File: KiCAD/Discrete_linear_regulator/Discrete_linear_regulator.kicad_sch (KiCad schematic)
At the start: 40 parts, among them J1 Conn_01x06, Q1 PZT2222AT3G, Q10 BC857, Q11 BC857, Q2 BC857, Q3 BC857, Q4 PZT2222AT3G, Q5 PZT2907AT3G, Q8 PZT2907AT3G, U1 LM4562

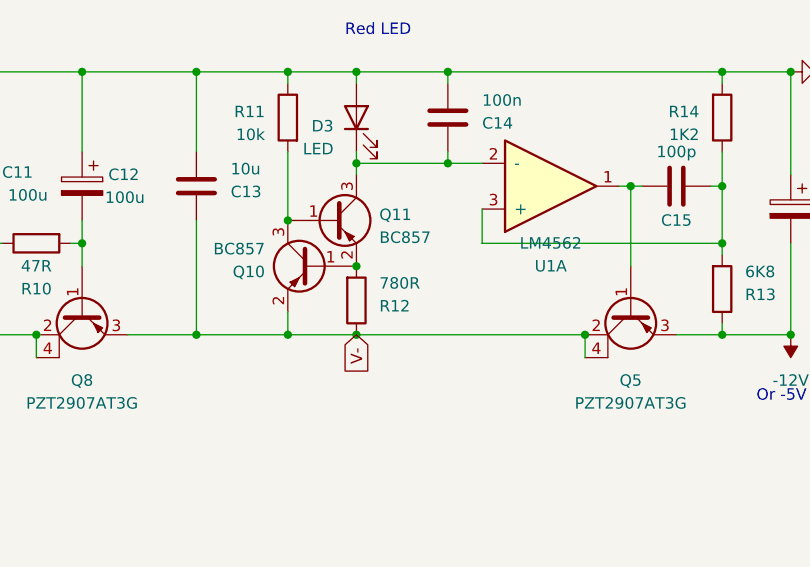
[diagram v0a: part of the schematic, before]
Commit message: Linear regulator schematic update
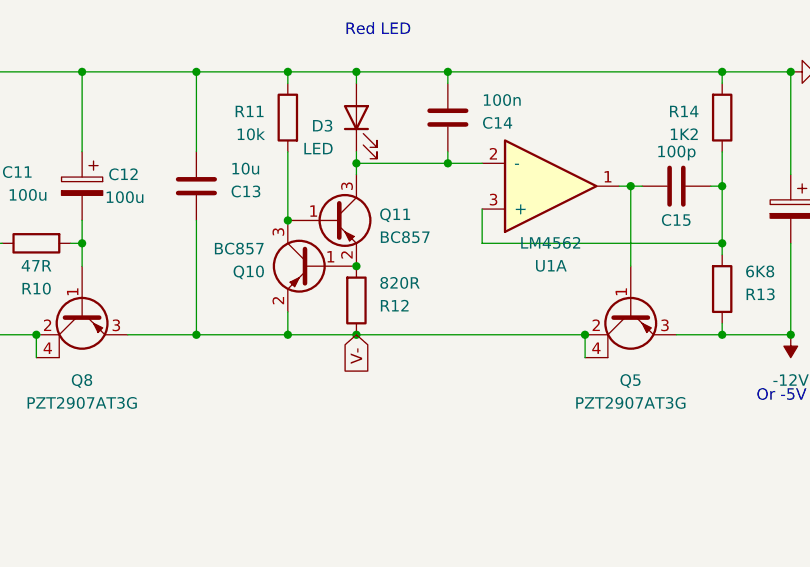
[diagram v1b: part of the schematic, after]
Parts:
- R12: value 780R -> 820R
- R13, R14, R6, R7: Datasheet2 (none) -> https://nl.mouser.com/ProductDetail/Susumu/RG1005P-272-D-T1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
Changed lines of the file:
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@@
       (effects (font (size 1.27 1.27)) hide)
     )
-    (property "Datasheet" "~" (at 102.87 104.14 0)
+    (property "Datasheet" "https://nl.mouser.com/ProductDetail/Vishay-Dale/CRCW040210K0FKEDC?qs=E3Y5ESvWgWPiNLcGzwCGPg%3D%3D" (at 102.87 104.14 0)
       (effects (font (size 1.27 1.27)) hide)
     )
@@
       (effects (font (size 1.27 1.27)) hide)
     )
-    (property "Datasheet" "~" (at 262.89 74.93 0)
+    (property "Datasheet" "https://nl.mouser.com/ProductDetail/Murata-Electronics/GRM155R71H104KE14D?qs=sGAEpiMZZMvsSlwiRhF8qkiosXznb836lYH0b0rR9OM%3D" (at 262.89 74.93 0)
       (effects (font (size 1.27 1.27)) hide)
     )
@@
       (effects (font (size 1.27 1.27)) hide)
     )
-    (property "Datasheet" "~" (at 262.89 67.31 0)
+    (property "Datasheet" "https://nl.mouser.com/ProductDetail/Murata-Electronics/GRM155R71H104KE14D?qs=sGAEpiMZZMvsSlwiRhF8qkiosXznb836lYH0b0rR9OM%3D" (at 262.89 67.31 0)
       (effects (font (size 1.27 1.27)) hide)
     )
@@
       (effects (font (size 1.27 1.27)) hide)
     )
-    (property "Datasheet" "~" (at 74.93 118.11 0)
+    (property "Datasheet" "https://nl.mouser.com/ProductDetail/YAGEO/RT0402FRE0747RL?qs=sGAEpiMZZMvdGkrng054t0q%2FxTkBpeSrrs0gjydReCc%3D" (at 74.93 118.11 0)
       (effects (font (size 1.27 1.27)) hide)
     )
@@
       (effects (font (size 1.27 1.27)) (justify left))
     )
-    (property "Value" "780R" (at 113.03 122.555 0)
+    (property "Value" "820R" (at 113.03 122.555 0)
       (effects (font (size 1.27 1.27)) (justify left))
     )
@@
       (effects (font (size 1.27 1.27)) hide)
     )
-    (property "Datasheet" "~" (at 110.49 124.46 0)
+    (property "Datasheet" "https://nl.mouser.com/ProductDetail/YAGEO/RT0402FRE07820RL?qs=iFuT%252BolKbR7tOecAWZmkmw%3D%3D" (at 110.49 124.46 0)
       (effects (font (size 1.27 1.27)) hide)
     )
@@
       (effects (font (size 1.27 1.27)) hide)
     )
-    (property "Datasheet" "~" (at 146.05 76.2 0)
+    (property "Datasheet" "https://nl.mouser.com/ProductDetail/KEMET/CBR04C101J5GACAUTO?qs=By6Nw2ByBD2z15b9CQ8m6A%3D%3D" (at 146.05 76.2 0)
       (effects (font (size 1.27 1.27)) hide)
     )
@@
       (effects (font (size 1.27 1.27)) hide)
     )
-    (property "Datasheet" "~" (at 146.05 111.76 0)
+    (property "Datasheet" "https://nl.mouser.com/ProductDetail/KEMET/CBR04C101J5GACAUTO?qs=By6Nw2ByBD2z15b9CQ8m6A%3D%3D" (at 146.05 111.76 0)
       (effects (font (size 1.27 1.27)) hide)
     )
@@
       (effects (font (size 1.27 1.27)) hide)
     )
-    (property "Datasheet" "~" (at 151.13 104.14 0)
+    (property "Datasheet" "https://nl.mouser.com/ProductDetail/Susumu/RR0510P-122-D?qs=nCAm%252BcMdy9x80DxeUz5E6w%3D%3D" (at 151.13 104.14 0)
+      (effects (font (size 1.27 1.27)) hide)
+    )
+    (property "Datasheet2" "https://nl.mouser.com/ProductDetail/Susumu/RG1005P-272-D-T10?qs=y7y%2FNpWpM9kYXyOrAmBBBw%3D%3D" (at 151.13 104.14 0)
       (effects (font (size 1.27 1.27)) hide)
     )
@@
       (effects (font (size 1.27 1.27)) hide)
     )
-    (property "Datasheet" "~" (at 62.23 123.19 0)
+    (property "Datasheet" "https://nl.mouser.com/ProductDetail/YAGEO/RT0402FRE07100RL?qs=sGAEpiMZZMvdGkrng054t%252BKCHBXLTLydY05E6nMrbFY%3D" (at 62.23 123.19 0)
       (effects (font (size 1.27 1.27)) hide)
     )
@@
       (effects (font (size 1.27 1.27)) hide)
     )
-    (property "Datasheet" "~" (at 62.23 111.76 0)
+    (property "Datasheet" "https://nl.mouser.com/ProductDetail/Vishay-Dale/CRCW0402100KFKEDC?qs=E3Y5ESvWgWPiKlL6PvtQMQ%3D%3D" (at 62.23 111.76 0)
       (effects (font (size 1.27 1.27)) hide)
     )
@@
       (effects (font (size 1.27 1.27)) hide)
     )
-    (property "Datasheet" "~" (at 151.13 123.19 0)
+    (property "Datasheet" "https://nl.mouser.com/ProductDetail/Susumu/RG1005P-682-D-T10?qs=v5GkGT6DDHhLDDYpYvRXHQ%3D%3D" (at 151.13 123.19 0)
+      (effects (font (size 1.27 1.27)) hide)
+    )
+    (property "Datasheet2" "https://nl.mouser.com/ProductDetail/Susumu/RG1005P-272-D-T10?qs=y7y%2FNpWpM9kYXyOrAmBBBw%3D%3D" (at 151.13 123.19 0)
       (effects (font (size 1.27 1.27)) hide)
     )
@@
       (effects (font (size 1.27 1.27)) hide)
     )
-    (property "Datasheet" "~" (at 151.13 64.77 0)
+    (property "Datasheet" "https://nl.mouser.com/ProductDetail/Susumu/RG1005P-682-D-T10?qs=v5GkGT6DDHhLDDYpYvRXHQ%3D%3D" (at 151.13 64.77 0)
+      (effects (font (size 1.27 1.27)) hide)
+    )
+    (property "Datasheet2" "https://nl.mouser.com/ProductDetail/Susumu/RG1005P-272-D-T10?qs=y7y%2FNpWpM9kYXyOrAmBBBw%3D%3D" (at 151.13 64.77 0)
       (effects (font (size 1.27 1.27)) hide)
     )
@@
       (effects (font (size 1.27 1.27)) hide)
     )
-    (property "Datasheet" "~" (at 151.13 83.82 0)
-      (effects (font (size 1.27 1.27)) hide)
-    )
+    (property "Datasheet" "https://nl.mouser.com/ProductDetail/Susumu/RR0510P-122-D?qs=nCAm%252BcMdy9x80DxeUz5E6w%3D%3D" (at 151.13 83.82 0)
+      (effects (font (size 1.27 1.27)) hide)
+    )
+    (property "Datasheet2" "https://nl.mouser.com/ProductDetail/Susumu/RG1005P-272-D-T10?qs=y7y%2FNpWpM9kYXyOrAmBBBw%3D%3D" (at 151.13 83.82 0)
+      (effects (font (size 1.27 1.27)) hide)
+    )

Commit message: Schematic update
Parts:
- removed Q10, Q11: BC857, Package_TO_SOT_SMD:SOT-23, symbol Transistor_BJT:BC857
- added Q10, Q11: BC847, Package_TO_SOT_SMD:SOT-23, symbol Transistor_BJT:BC847
- R14: Datasheet2 https://nl.mouser.com/ProductDetail/Susumu/RG1005P-272-D-T1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 -> https://nl.mouser.com/ProductDetail/Susumu/RG1005P-152-D-T1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
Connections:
- net V-: now also Q10.2 (E)
- net at R12.2: now also Q10.1 (B), Q11.2 (E)
- net at R11.2: now also Q10.3 (C), Q11.1 (B)
- net at C14.1, D3.1 (K), U1.2 (-): now also Q11.3 (C)
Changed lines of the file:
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@@
   (junction (at 74.93 59.69) (diameter 0) (color 0 0 0 0)
   )
+  (junction (at 110.49 120.65) (diameter 0) (color 0 0 0 0)
+  )
   (junction (at 62.23 59.69) (diameter 0) (color 0 0 0 0)
   )
@@
   (junction (at 102.87 99.06) (diameter 0) (color 0 0 0 0)
   )
+  (junction (at 158.75 88.9) (diameter 0) (color 0 0 0 0)
+  )
+  (junction (at 102.87 59.69) (diameter 0) (color 0 0 0 0)
+  )
+  (junction (at 158.75 59.69) (diameter 0) (color 0 0 0 0)
+  )
+  (junction (at 158.75 128.27) (diameter 0) (color 0 0 0 0)
+  )
+  (junction (at 135.89 59.69) (diameter 0) (color 0 0 0 0)
+  )
+  (junction (at 151.13 59.69) (diameter 0) (color 0 0 0 0)
+  )
+  (junction (at 151.13 76.2) (diameter 0) (color 0 0 0 0)
+  )
+  (junction (at 102.87 72.39) (diameter 0) (color 0 0 0 0)
+  )
+  (junction (at 110.49 88.9) (diameter 0) (color 0 0 0 0)
+  )
+  (junction (at 62.23 69.85) (diameter 0) (color 0 0 0 0)
+  )
+  (junction (at 120.65 88.9) (diameter 0) (color 0 0 0 0)
+  )
+  (junction (at 151.13 88.9) (diameter 0) (color 0 0 0 0)
+  )
+  (junction (at 110.49 59.69) (diameter 0) (color 0 0 0 0)
+  )
+  (junction (at 67.31 99.06) (diameter 0) (color 0 0 0 0)
+  )
+  (junction (at 67.31 69.85) (diameter 0) (color 0 0 0 0)
+  )
+  (junction (at 110.49 128.27) (diameter 0) (color 0 0 0 0)
+  )
+  (junction (at 151.13 111.76) (diameter 0) (color 0 0 0 0)
+  )
+  (junction (at 80.01 118.11) (diameter 0) (color 0 0 0 0)
+  )
+  (junction (at 92.71 99.06) (diameter 0) (color 0 0 0 0)
+  )
+  (junction (at 110.49 78.74) (diameter 0) (color 0 0 0 0)
+  )
+  (junction (at 92.71 59.69) (diameter 0) (color 0 0 0 0)
+  )
+  (junction (at 120.65 78.74) (diameter 0) (color 0 0 0 0)
+  )
+  (junction (at 151.13 69.85) (diameter 0) (color 0 0 0 0)
+  )
+  (junction (at 102.87 128.27) (diameter 0) (color 0 0 0 0)
+  )
+  (junction (at 262.89 71.12) (diameter 0) (color 0 0 0 0)
+  )
+  (junction (at 151.13 118.11) (diameter 0) (color 0 0 0 0)
+  )
+  (junction (at 92.71 88.9) (diameter 0) (color 0 0 0 0)
+  )
+  (junction (at 120.65 99.06) (diameter 0) (color 0 0 0 0)
+  )
+  (junction (at 74.93 128.27) (diameter 0) (color 0 0 0 0)
+  )
+  (junction (at 67.31 118.11) (diameter 0) (color 0 0 0 0)
+  )
   (junction (at 102.87 115.57) (diameter 0) (color 0 0 0 0)
-  )
-  (junction (at 158.75 88.9) (diameter 0) (color 0 0 0 0)
-  )
-  (junction (at 102.87 59.69) (diameter 0) (color 0 0 0 0)
-  )
-  (junction (at 158.75 59.69) (diameter 0) (color 0 0 0 0)
-  )
-  (junction (at 158.75 128.27) (diameter 0) (color 0 0 0 0)
-  )
-  (junction (at 135.89 59.69) (diameter 0) (color 0 0 0 0)
-  )
-  (junction (at 151.13 59.69) (diameter 0) (color 0 0 0 0)
-  )
-  (junction (at 151.13 76.2) (diameter 0) (color 0 0 0 0)
-  )
-  (junction (at 102.87 72.39) (diameter 0) (color 0 0 0 0)
-  )
-  (junction (at 110.49 88.9) (diameter 0) (color 0 0 0 0)
-  )
-  (junction (at 62.23 69.85) (diameter 0) (color 0 0 0 0)
-  )
-  (junction (at 120.65 88.9) (diameter 0) (color 0 0 0 0)
-  )
-  (junction (at 151.13 88.9) (diameter 0) (color 0 0 0 0)
-  )
-  (junction (at 110.49 59.69) (diameter 0) (color 0 0 0 0)
-  )
-  (junction (at 67.31 99.06) (diameter 0) (color 0 0 0 0)
-  )
-  (junction (at 67.31 69.85) (diameter 0) (color 0 0 0 0)
-  )
-  (junction (at 110.49 128.27) (diameter 0) (color 0 0 0 0)
-  )
-  (junction (at 151.13 111.76) (diameter 0) (color 0 0 0 0)
-  )
-  (junction (at 80.01 118.11) (diameter 0) (color 0 0 0 0)
-  )
-  (junction (at 92.71 99.06) (diameter 0) (color 0 0 0 0)
-  )
-  (junction (at 110.49 78.74) (diameter 0) (color 0 0 0 0)
-  )
-  (junction (at 92.71 59.69) (diameter 0) (color 0 0 0 0)
-  )
-  (junction (at 120.65 78.74) (diameter 0) (color 0 0 0 0)
-  )
-  (junction (at 151.13 69.85) (diameter 0) (color 0 0 0 0)
-  )
-  (junction (at 102.87 128.27) (diameter 0) (color 0 0 0 0)
-  )
-  (junction (at 262.89 71.12) (diameter 0) (color 0 0 0 0)
-  )
-  (junction (at 151.13 118.11) (diameter 0) (color 0 0 0 0)
-  )
-  (junction (at 110.49 120.65) (diameter 0) (color 0 0 0 0)
-  )
-  (junction (at 92.71 88.9) (diameter 0) (color 0 0 0 0)
-  )
-  (junction (at 120.65 99.06) (diameter 0) (color 0 0 0 0)
-  )
-  (junction (at 74.93 128.27) (diameter 0) (color 0 0 0 0)
-  )
-  (junction (at 67.31 118.11) (diameter 0) (color 0 0 0 0)
   )
   (wire (pts (xy 135.89 130.81) (xy 135.89 128.27))
@@
     )
   )
-  (symbol (lib_id "Transistor_BJT:BC857") (at 105.41 120.65 0) (mirror y) (unit 1)
-    (in_bom yes) (on_board yes) (dnp no) (fields_autoplaced)
-    (property "Reference" "Q10" (at 100.33 121.285 0)
-      (effects (font (size 1.27 1.27)) (justify left))
-    )
-    (property "Value" "BC857" (at 100.33 118.745 0)
-      (effects (font (size 1.27 1.27)) (justify left))
-    )
-    (property "Footprint" "Package_TO_SOT_SMD:SOT-23" (at 100.33 122.555 0)
-      (effects (font (size 1.27 1.27) italic) (justify left) hide)
-    )
-    (property "Datasheet" "" (at 105.41 120.65 0)
-      (effects (font (size 1.27 1.27)) (justify left) hide)
-    )
-    (pin "1")
-    (pin "2")
-    (pin "3")
-    (instances
-      (project "Discrete_linear_regulator"
-        (path "/19504711-657f-4df2-b2e9-322b7e64e4f7"
-          (reference "Q10") (unit 1)
-        )
-      )
-    )
-  )
   (symbol (lib_id "Connector_Generic:Conn_01x06") (at 20.32 71.12 0) (mirror y) (unit 1)
     (in_bom yes) (on_board yes) (dnp no)
@@
         (path "/19504711-657f-4df2-b2e9-322b7e64e4f7"
           (reference "#PWR015") (unit 1)
+        )
+      )
+    )
+  )
+  (symbol (lib_id "Transistor_BJT:BC847") (at 107.95 115.57 0) (unit 1)
+    (in_bom yes) (on_board yes) (dnp no)
+    (property "Reference" "Q11" (at 113.665 114.935 0)
+      (effects (font (size 1.27 1.27)) (justify left))
+    )
+    (property "Value" "BC847" (at 113.665 117.475 0)
+      (effects (font (size 1.27 1.27)) (justify left))
+    )
+    (property "Footprint" "Package_TO_SOT_SMD:SOT-23" (at 113.03 117.475 0)
+      (effects (font (size 1.27 1.27) italic) (justify left) hide)
+    )
+    (property "Datasheet" "https://nl.mouser.com/ProductDetail/Nexperia/BC847C215?qs=me8TqzrmIYVnv3C18%2Fxa3Q%3D%3D" (at 107.95 115.57 0)
+      (effects (font (size 1.27 1.27)) (justify left) hide)
+    )
+    (pin "1")
+    (pin "2")
+    (pin "3")
+    (instances
+      (project "Discrete_linear_regulator"
+        (path "/19504711-657f-4df2-b2e9-322b7e64e4f7"
+          (reference "Q11") (unit 1)
         )
       )
@@
     )
   )
-  (symbol (lib_id "Transistor_BJT:BC857") (at 107.95 115.57 0) (unit 1)
-    (in_bom yes) (on_board yes) (dnp no)
-    (property "Reference" "Q11" (at 113.03 114.935 0)
-      (effects (font (size 1.27 1.27)) (justify left))
-    )
-    (property "Value" "BC857" (at 113.03 117.475 0)
-      (effects (font (size 1.27 1.27)) (justify left))
-    )
-    (property "Footprint" "Package_TO_SOT_SMD:SOT-23" (at 113.03 117.475 0)
-      (effects (font (size 1.27 1.27) italic) (justify left) hide)
-    )
-    (property "Datasheet" "" (at 107.95 115.57 0)
-      (effects (font (size 1.27 1.27)) (justify left) hide)
-    )
-    (pin "1")
-    (pin "2")
-    (pin "3")
-    (instances
-      (project "Discrete_linear_regulator"
-        (path "/19504711-657f-4df2-b2e9-322b7e64e4f7"
-          (reference "Q11") (unit 1)
-        )
-      )
-    )
-  )
   (symbol (lib_id "power:GND") (at 25.4 76.2 90) (unit 1)
     (in_bom yes) (on_board yes) (dnp no) (fields_autoplaced)
@@
       (effects (font (size 1.27 1.27)) hide)
     )
-    (property "Datasheet2" "https://nl.mouser.com/ProductDetail/Susumu/RG1005P-272-D-T10?qs=y7y%2FNpWpM9kYXyOrAmBBBw%3D%3D" (at 151.13 104.14 0)
+    (property "Datasheet2" "https://nl.mouser.com/ProductDetail/Susumu/RG1005P-152-D-T10?qs=y7y%2FNpWpM9nW0HJrZd%252BQRA%3D%3D" (at 151.13 104.14 0)
       (effects (font (size 1.27 1.27)) hide)
     )
@@
         )
       )
+    )
+  )
+  (symbol (lib_id "Transistor_BJT:BC847") (at 105.41 120.65 0) (mirror y) (unit 1)
+    (in_bom yes) (on_board yes) (dnp no)
+    (property "Reference" "Q10" (at 99.695 120.015 0)
+      (effects (font (size 1.27 1.27)) (justify left))
+    )
+    (property "Value" "BC847" (at 99.695 122.555 0)
+      (effects (font (size 1.27 1.27)) (justify left))
+    )
+    (property "Footprint" "Package_TO_SOT_SMD:SOT-23" (at 100.33 122.555 0)
+      (effects (font (size 1.27 1.27) italic) (justify left) hide)
+    )
+    (property "Datasheet" "https://nl.mouser.com/ProductDetail/Nexperia/BC847C215?qs=me8TqzrmIYVnv3C18%2Fxa3Q%3D%3D" (at 105.41 120.65 0)
+      (effects (font (size 1.27 1.27)) (justify left) hide)
+    )
+    (pin "1")
+    (pin "2")
+    (pin "3")
+    (instances
+      (project "Discrete_linear_regulator"
+        (path "/19504711-657f-4df2-b2e9-322b7e64e4f7"
+          (reference "Q10") (unit 1)
+        )
+      )

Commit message: update linear
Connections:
- net at C14.1, D3.1 (K), Q11.3 (C): now also U1.6 (-); no longer U1.2 (-)
- net at C4.1, D1.2 (A), Q3.3 (C): now also U1.2 (-); no longer U1.6 (-)
- net at C2.2, Q4.1: now also U1.1; no longer U1.7
- net at C2.1, R6.2, R7.1: now also U1.3 (+); no longer U1.5 (+)
- net at C15.2, Q5.1: now also U1.7; no longer U1.1
- net at C15.1, R13.2, R14.1: now also U1.5 (+); no longer U1.3 (+)
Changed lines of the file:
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@@
     )
   )
-  (symbol (lib_id "Audio_DSP:LM4562") (at 130.81 111.76 0) (mirror x) (unit 1)
+  (symbol (lib_id "Audio_DSP:LM4562") (at 130.81 111.76 0) (mirror x) (unit 2)
     (in_bom yes) (on_board yes) (dnp no)
     (property "Reference" "U1" (at 132.08 120.65 0)
@@
       (project "Discrete_linear_regulator"
         (path "/19504711-657f-4df2-b2e9-322b7e64e4f7"
-          (reference "U1") (unit 1)
+          (reference "U1") (unit 2)
         )
       )
@@
     )
   )
-  (symbol (lib_id "Audio_DSP:LM4562") (at 130.81 76.2 0) (unit 2)
+  (symbol (lib_id "Audio_DSP:LM4562") (at 130.81 76.2 0) (unit 1)
     (in_bom yes) (on_board yes) (dnp no)
     (property "Reference" "U1" (at 132.08 67.31 0)
@@
       (project "Discrete_linear_regulator"
         (path "/19504711-657f-4df2-b2e9-322b7e64e4f7"
-          (reference "U1") (unit 2)
-        )
-      )
+          (reference "U1") (unit 1)
+        )
+      )

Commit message: update linear and gerbers
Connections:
- net at C14.1, D3.1 (K), Q11.3 (C): now also U1.5 (+); no longer U1.6 (-)
- net at C4.1, D1.2 (A), Q3.3 (C): now also U1.3 (+); no longer U1.2 (-)
- net at C2.1, R6.2, R7.1: now also U1.2 (-); no longer U1.3 (+)
- net at C15.1, R13.2, R14.1: now also U1.6 (-); no longer U1.5 (+)
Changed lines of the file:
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@@
     )
   )
-  (symbol (lib_id "Audio_DSP:LM4562") (at 130.81 111.76 0) (mirror x) (unit 2)
-    (in_bom yes) (on_board yes) (dnp no)
-    (property "Reference" "U1" (at 132.08 120.65 0)
-      (effects (font (size 1.27 1.27)))
-    )
-    (property "Value" "LM4562" (at 132.08 118.11 0)
-      (effects (font (size 1.27 1.27)))
-    )
-    (property "Footprint" "Package_SO:SOIC-8_3.9x4.9mm_P1.27mm" (at 132.08 118.11 0)
-      (effects (font (size 1.27 1.27)) hide)
-    )
-    (property "Datasheet" "https://nl.farnell.com/texas-instruments/lm4562max-nopb/audio-amplifier-55mhz-20v-us-soic/dp/3004534?st=lm4562" (at 132.08 118.11 0)
+  (symbol (lib_id "Audio_DSP:LM4562") (at 130.81 111.76 0) (unit 2)
+    (in_bom yes) (on_board yes) (dnp no)
+    (property "Reference" "U1" (at 132.08 102.87 0)
+      (effects (font (size 1.27 1.27)))
+    )
+    (property "Value" "LM4562" (at 132.08 105.41 0)
+      (effects (font (size 1.27 1.27)))
+    )
+    (property "Footprint" "Package_SO:SOIC-8_3.9x4.9mm_P1.27mm" (at 132.08 105.41 0)
+      (effects (font (size 1.27 1.27)) hide)
+    )
+    (property "Datasheet" "https://nl.farnell.com/texas-instruments/lm4562max-nopb/audio-amplifier-55mhz-20v-us-soic/dp/3004534?st=lm4562" (at 132.08 105.41 0)
       (effects (font (size 1.27 1.27)) hide)
     )
@@
     )
   )
-  (symbol (lib_id "Audio_DSP:LM4562") (at 130.81 76.2 0) (unit 1)
-    (in_bom yes) (on_board yes) (dnp no)
-    (property "Reference" "U1" (at 132.08 67.31 0)
-      (effects (font (size 1.27 1.27)))
-    )
-    (property "Value" "LM4562" (at 132.08 69.85 0)
-      (effects (font (size 1.27 1.27)))
-    )
-    (property "Footprint" "Package_SO:SOIC-8_3.9x4.9mm_P1.27mm" (at 132.08 69.85 0)
-      (effects (font (size 1.27 1.27)) hide)
-    )
-    (property "Datasheet" "https://nl.farnell.com/texas-instruments/lm4562max-nopb/audio-amplifier-55mhz-20v-us-soic/dp/3004534?st=lm4562" (at 132.08 69.85 0)
-      (effects (font (size 1.27 1.27)) hide)
-    )
+  (symbol (lib_id "Audio_DSP:LM4562") (at 130.81 76.2 0) (mirror x) (unit 1)
+    (in_bom yes) (on_board yes) (dnp no)
+    (property "Reference" "U1" (at 132.08 85.09 0)
+      (effects (font (size 1.27 1.27)))
+    )
+    (property "Value" "LM4562" (at 132.08 82.55 0)
+      (effects (font (size 1.27 1.27)))
+    )
+    (property "Footprint" "Package_SO:SOIC-8_3.9x4.9mm_P1.27mm" (at 132.08 82.55 0)
+      (effects (font (size 1.27 1.27)) hide)
+    )
+    (property "Datasheet" "https://nl.farnell.com/texas-instruments/lm4562max-nopb/audio-amplifier-55mhz-20v-us-soic/dp/3004534?st=lm4562" (at 132.08 82.55 0)
+      (effects (font (size 1.27 1.27)) hide)
+    )
